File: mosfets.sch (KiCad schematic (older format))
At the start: 79 parts, among them P5 TERMINAL_BLOCK, P6 TERMINAL_BLOCK, Q1 2N7002P, Q10 2N7002P, Q11 2N7002P, Q12 BC846BPDW1, Q13 BC846BPDW1, Q14 SI2318CDS-T1-GE3, Q15 IRFB7545PbF, Q16 2N7002P, Q17 2N7002P, Q18 BC846BPDW1, Q19 BC846BPDW1, Q2 2N7002P, Q20 SI2318CDS-T1-GE3, Q21 IRFB7545PbF, Q3 2N7002P, Q4 BC846BPDW1, Q5 BC846BPDW1, Q6 BC846BPDW1, Q7 IRFB7545PbF, Q8 SI2318CDS-T1-GE3, Q9 IRFB7545PbF

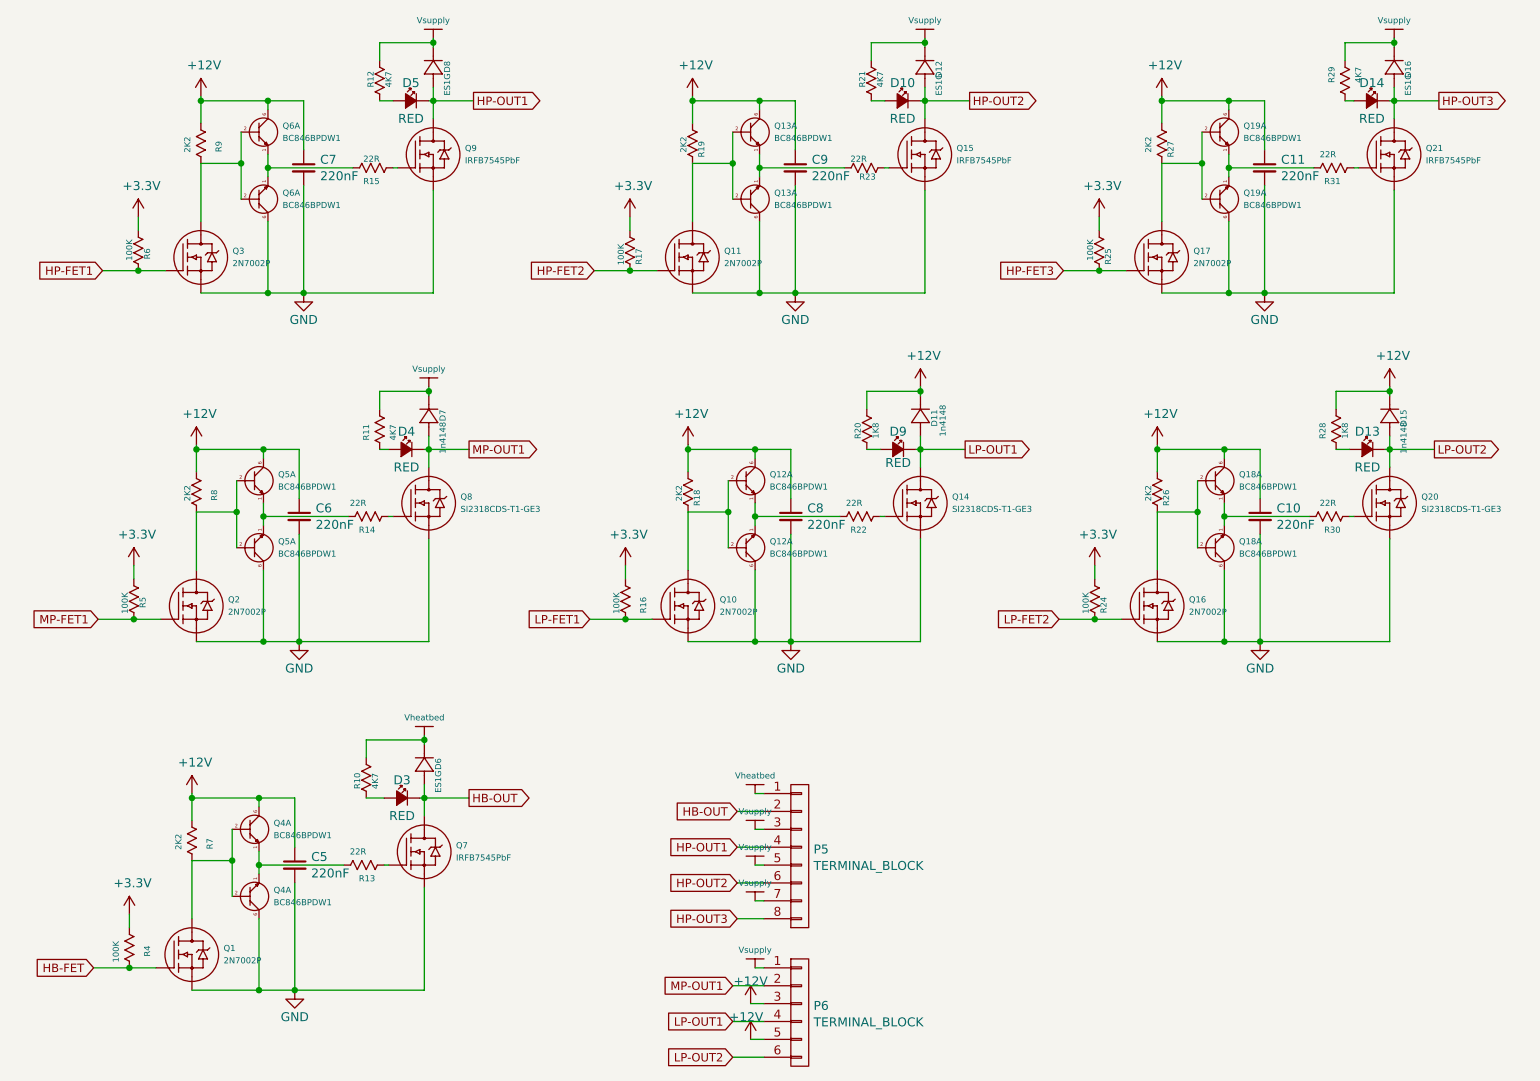
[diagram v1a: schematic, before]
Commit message: - Fix si2318 pinout - Fix slot problem introduced with attribute changes
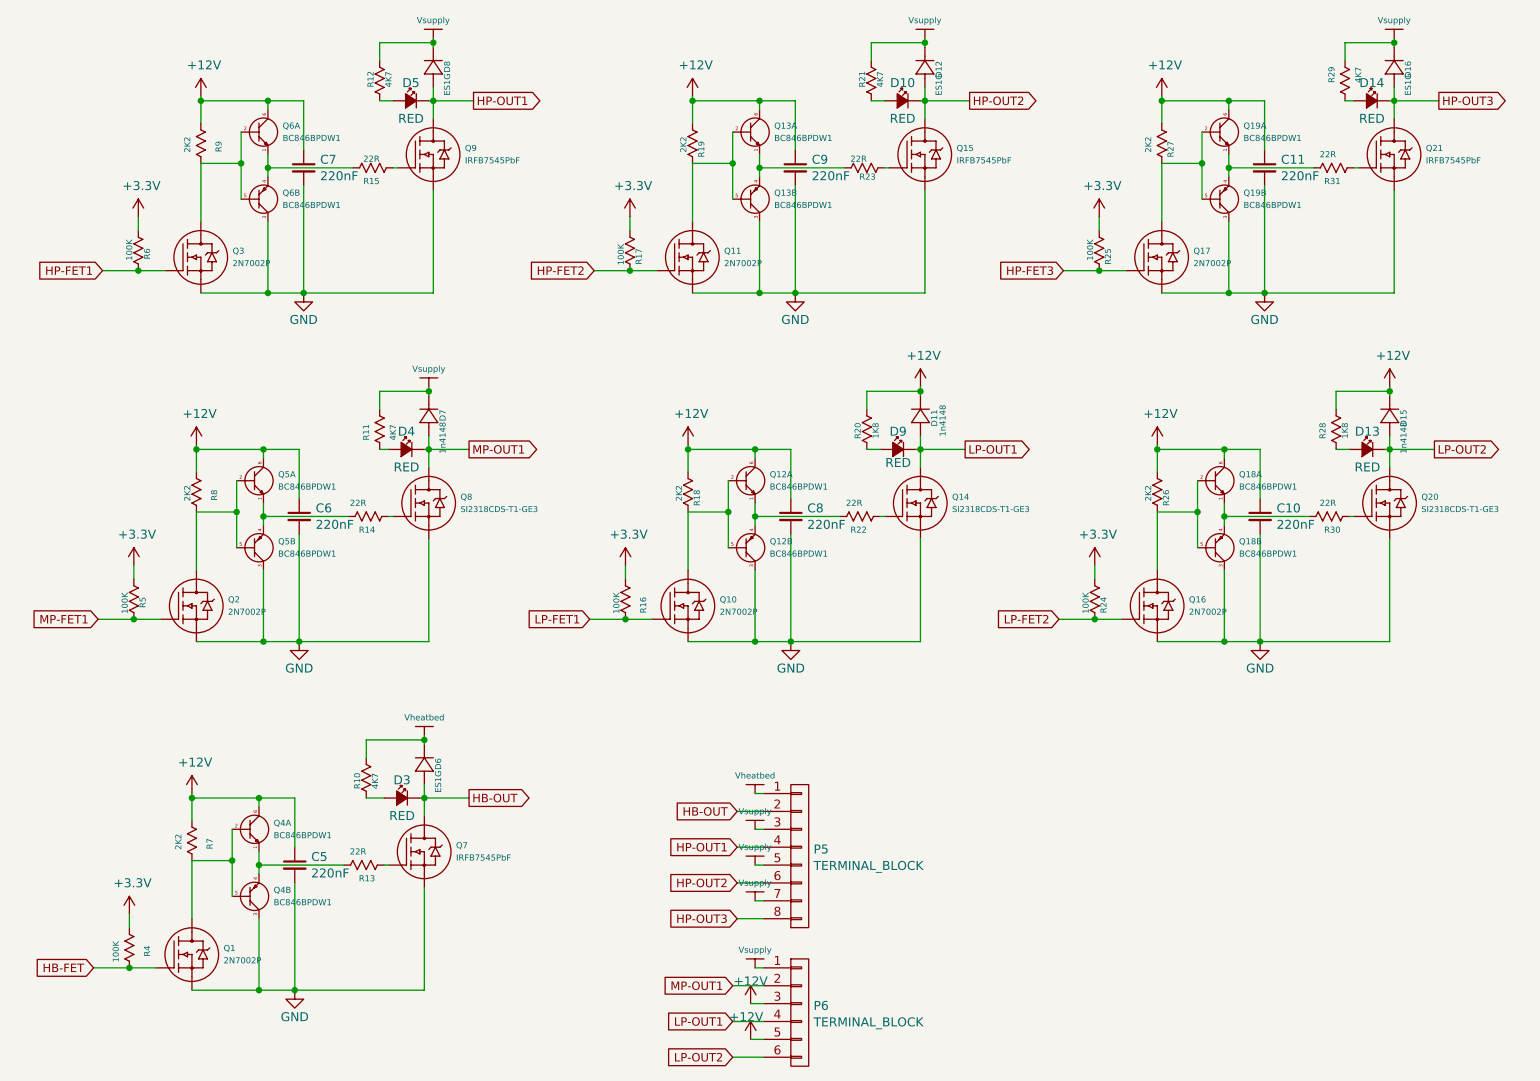
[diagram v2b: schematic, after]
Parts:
- removed Q14, Q20, Q8: SI2318CDS-T1-GE3, sot:SOT23_3L, symbol DMN3404L
- added Q14, Q20, Q8: SI2318CDS-T1-GE3, sot:SOT23_3L, symbol si2318cds
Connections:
- net GND: now also Q12.3 (C), Q13.3 (C), Q18.3 (C), Q19.3 (C), Q4.3 (C), Q5.3 (C), Q6.3 (C), Q14.2 (S), Q20.2 (S), Q8.2 (S); no longer Q12.6 (C), Q13.6 (C), Q18.6 (C), Q19.6 (C), Q4.6 (C), Q5.6 (C), Q6.6 (C)
- net LP-OUT1: now also Q14.3 (D)
- net LP-OUT2: now also Q20.3 (D)
- net MP-OUT1: now also Q8.3 (D)
- net at Q3.3 (D), Q6.2 (B), R9.1: now also Q6.5 (B); no longer Q6.2 (B)
- net at Q6.1 (E), R15.1: now also Q6.4 (E); no longer Q6.1 (E)
- net at Q11.3 (D), Q13.2 (B), R19.1: now also Q13.5 (B); no longer Q13.2 (B)
- net at Q13.1 (E), R23.1: now also Q13.4 (E); no longer Q13.1 (E)
- net at Q17.3 (D), Q19.2 (B), R27.1: now also Q19.5 (B); no longer Q19.2 (B)
- net at Q19.1 (E), R31.1: now also Q19.4 (E); no longer Q19.1 (E)
- net at Q1.3 (D), Q4.2 (B), R7.1: now also Q4.5 (B); no longer Q4.2 (B)
- net at Q4.1 (E), R13.1: now also Q4.4 (E); no longer Q4.1 (E)
- net at Q2.3 (D), Q5.2 (B), R8.1: now also Q5.5 (B); no longer Q5.2 (B)
- net at Q5.1 (E), R14.1: now also Q5.4 (E); no longer Q5.1 (E)
- net at R14.2: now also Q8.1 (G)
- net at Q10.3 (D), Q12.2 (B), R18.1: now also Q12.5 (B); no longer Q12.2 (B)
- net at Q12.1 (E), R22.1: now also Q12.4 (E); no longer Q12.1 (E)
- net at R22.2: now also Q14.1 (G)
- net at Q16.3 (D), Q18.2 (B), R26.1: now also Q18.5 (B); no longer Q18.2 (B)
- net at Q18.1 (E), R30.1: now also Q18.4 (E); no longer Q18.1 (E)
- net at R30.2: now also Q20.1 (G)
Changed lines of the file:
@@
 $Comp
 L BC846BPDW1 Q6
-U 1 1 568AF2DE
+U 2 1 568AF2DE
 P 2050 1625
 F 0 "Q6" H 2282 1715 34  0000 L CNN
@@
 F 4 "BC846BPDW1T1G" H 2050 1625 135 0001 L CNN "ManufacturerNo"
 F 5 "On Semiconductor" H 2050 1625 135 0001 L CNN "Manufacturer"
-	1    2050 1625
+	2    2050 1625
 	1    0    0    1
 $EndComp
@@
 $EndComp
 $Comp
-L Vsupply #P10
+L Vsupply #P11
 U 1 1 568AFFE8
 P 3125 700
-F 0 "#P10" H 3125 700 60  0001 C CNN
+F 0 "#P11" H 3125 700 60  0001 C CNN
 F 1 "Vsupply" H 3125 650 34  0000 C CNN
 F 2 "" H 3125 700 60  0000 C CNN
@@
 $Comp
 L BC846BPDW1 Q19
-U 1 1 568B2428
+U 2 1 568B2428
 P 7425 1625
 F 0 "Q19" H 7657 1715 34  0000 L CNN
@@
 F 4 "BC846BPDW1T1G" H 7425 1625 135 0001 L CNN "ManufacturerNo"
 F 5 "On Semiconductor" H 7425 1625 135 0001 L CNN "Manufacturer"
-	1    7425 1625
+	2    7425 1625
 	1    0    0    1
 $EndComp
@@
 $EndComp
 $Comp
-L Vsupply #P17
+L Vsupply #P18
 U 1 1 568B248A
 P 8500 700
-F 0 "#P17" H 8500 700 60  0001 C CNN
+F 0 "#P18" H 8500 700 60  0001 C CNN
 F 1 "Vsupply" H 8500 650 34  0000 C CNN
 F 2 "" H 8500 700 60  0000 C CNN
@@
 $Comp
 L BC846BPDW1 Q4
-U 1 1 568B41D4
+U 2 1 568B41D4
 P 2000 5525
 F 0 "Q4" H 2232 5615 34  0000 L CNN
@@
 F 4 "On Semiconductor" H 2000 5525 135 0001 L CNN "Manufacturer"
 F 5 "BC846BPDW1T1G" H 2000 5525 135 0001 L CNN "ManufacturerNo"
-	1    2000 5525
+	2    2000 5525
 	1    0    0    1
 $EndComp
@@
 $EndComp
 $Comp
-L Vheatbed #P8
+L Vheatbed #P9
 U 1 1 568B479B
 P 3075 4600
-F 0 "#P8" H 3075 4600 60  0001 C CNN
+F 0 "#P9" H 3075 4600 60  0001 C CNN
 F 1 "Vheatbed" H 3075 4550 34  0000 C CNN
 F 2 "" H 3075 4600 60  0000 C CNN
@@
 $Comp
 L BC846BPDW1 Q5
-U 1 1 568B79AD
+U 2 1 568B79AD
 P 2025 3575
 F 0 "Q5" H 2257 3665 34  0000 L CNN
@@
 F 4 "BC846BPDW1T1G" H 2025 3575 135 0001 L CNN "ManufacturerNo"
 F 5 "On Semiconductor" H 2025 3575 135 0001 L CNN "Manufacturer"
-	1    2025 3575
+	2    2025 3575
 	1    0    0    1
 $EndComp
@@
 $EndComp
 $Comp
-L Vsupply #P9
+L Vsupply #P10
 U 1 1 568B7A06
 P 3100 2650
-F 0 "#P9" H 3100 2650 60  0001 C CNN
+F 0 "#P10" H 3100 2650 60  0001 C CNN
 F 1 "Vsupply" H 3100 2600 34  0000 C CNN
 F 2 "" H 3100 2650 60  0000 C CNN
@@
 $Comp
 L BC846BPDW1 Q12
-U 1 1 568B7A20
+U 2 1 568B7A20
 P 4775 3575
 F 0 "Q12" H 5007 3665 34  0000 L CNN
@@
 F 4 "BC846BPDW1T1G" H 4775 3575 135 0001 L CNN "ManufacturerNo"
 F 5 "On Semiconductor" H 4775 3575 135 0001 L CNN "Manufacturer"
-	1    4775 3575
+	2    4775 3575
 	1    0    0    1
 $EndComp
@@
 $Comp
 L BC846BPDW1 Q18
-U 1 1 568B7A93
+U 2 1 568B7A93
 P 7400 3575
 F 0 "Q18" H 7632 3665 34  0000 L CNN
@@
 F 4 "BC846BPDW1T1G" H 7400 3575 135 0001 L CNN "ManufacturerNo"
 F 5 "On Semiconductor" H 7400 3575 135 0001 L CNN "Manufacturer"
-	1    7400 3575
+	2    7400 3575
 	1    0    0    1
 $EndComp
@@
 $EndComp
 $Comp
-L DMN3404L Q8
-U 1 1 568B81E9
-P 2900 3650
-F 0 "Q8" H 3277 3885 34  0000 L CNN
-F 1 "SI2318CDS-T1-GE3" H 3277 3816 34  0000 L CNN
-F 2 "sot:SOT23_3L" H 2900 3650 60  0001 C CNN
-F 3 "" H 2900 3650 60  0000 C CNN
-F 4 "SI2318CDS-T1-GE3" H 2900 3650 135 0001 L CNN "ManufacturerNo"
-F 5 "Vishay" H 2900 3650 135 0001 L CNN "Manufacturer"
-	1    2900 3650
-	1    0    0    -1
-$EndComp
-$Comp
 L 1n4148-RESCUE-rados D11
 U 1 1 568B8B88
@@
 	1    8525 3075
 	0    -1   -1   0
-$EndComp
-$Comp
-L DMN3404L Q14
-U 1 1 568B9231
-P 5650 3650
-F 0 "Q14" H 6027 3885 34  0000 L CNN
-F 1 "SI2318CDS-T1-GE3" H 6027 3816 34  0000 L CNN
-F 2 "sot:SOT23_3L" H 5650 3650 60  0001 C CNN
-F 3 "" H 5650 3650 60  0000 C CNN
-F 4 "SI2318CDS-T1-GE3" H 5650 3650 135 0001 L CNN "ManufacturerNo"
-F 5 "Vishay" H 5650 3650 135 0001 L CNN "Manufacturer"
-	1    5650 3650
-	1    0    0    -1
-$EndComp
-$Comp
-L DMN3404L Q20
-U 1 1 568B9365
-P 8275 3650
-F 0 "Q20" H 8652 3885 34  0000 L CNN
-F 1 "SI2318CDS-T1-GE3" H 8652 3816 34  0000 L CNN
-F 2 "sot:SOT23_3L" H 8275 3650 60  0001 C CNN
-F 3 "" H 8275 3650 60  0000 C CNN
-F 4 "SI2318CDS-T1-GE3" H 8275 3650 135 0001 L CNN "ManufacturerNo"
-F 5 "Vishay" H 8275 3650 135 0001 L CNN "Manufacturer"
-	1    8275 3650
-	1    0    0    -1
 $EndComp
 $Comp
@@
 $EndComp
 $Comp
-L Vheatbed #P11
+L Vheatbed #P12
 U 1 1 568B0A81
 P 4925 4925
-F 0 "#P11" H 4925 4925 60  0001 C CNN
+F 0 "#P12" H 4925 4925 60  0001 C CNN
 F 1 "Vheatbed" H 4925 4875 34  0000 C CNN
 F 2 "" H 4925 4925 60  0000 C CNN
@@
 $EndComp
 $Comp
-L Vsupply #P12
+L Vsupply #P13
 U 1 1 568B0DA2
 P 4925 5125
-F 0 "#P12" H 4925 5125 60  0001 C CNN
+F 0 "#P13" H 4925 5125 60  0001 C CNN
 F 1 "Vsupply" H 4925 5075 34  0000 C CNN
 F 2 "" H 4925 5125 60  0000 C CNN
@@
 $EndComp
 $Comp
-L Vsupply #P13
+L Vsupply #P14
 U 1 1 568B1161
 P 4925 5325
-F 0 "#P13" H 4925 5325 60  0001 C CNN
+F 0 "#P14" H 4925 5325 60  0001 C CNN
 F 1 "Vsupply" H 4925 5275 34  0000 C CNN
 F 2 "" H 4925 5325 60  0000 C CNN
@@
 HP-OUT1
 $Comp
-L Vsupply #P14
+L Vsupply #P15
 U 1 1 568BBE8C
 P 4925 5525
-F 0 "#P14" H 4925 5525 60  0001 C CNN
+F 0 "#P15" H 4925 5525 60  0001 C CNN
 F 1 "Vsupply" H 4925 5475 34  0000 C CNN
 F 2 "" H 4925 5525 60  0000 C CNN
@@
 HP-OUT3
 $Comp
-L Vsupply #P15
+L Vsupply #P16
 U 1 1 568BDAE4
 P 4925 5900
-F 0 "#P15" H 4925 5900 60  0001 C CNN
+F 0 "#P16" H 4925 5900 60  0001 C CNN
 F 1 "Vsupply" H 4925 5850 34  0000 C CNN
 F 2 "" H 4925 5900 60  0000 C CNN
@@
 $EndComp
 $Comp
-L Vsupply #P16
+L Vsupply #P17
 U 1 1 568B1D38
 P 5875 700
-F 0 "#P16" H 5875 700 60  0001 C CNN
+F 0 "#P17" H 5875 700 60  0001 C CNN
 F 1 "Vsupply" H 5875 650 34  0000 C CNN
 F 2 "" H 5875 700 60  0000 C CNN
@@
 $Comp
 L BC846BPDW1 Q13
-U 1 1 568B1CD6
+U 2 1 568B1CD6
 P 4800 1625
 F 0 "Q13" H 5032 1715 34  0000 L CNN
@@
 F 4 "BC846BPDW1T1G" H 4800 1625 135 0001 L CNN "ManufacturerNo"
 F 5 "On Semiconductor" H 4800 1625 135 0001 L CNN "Manufacturer"
-	1    4800 1625
+	2    4800 1625
 	1    0    0    1
 $EndComp
@@
 	1    0    0    -1
 $EndComp
+$Comp
+L si2318cds Q8
+U 1 1 56EAF7B5
+P 2900 3650
+F 0 "Q8" H 3277 3884 34  0000 L CNN
+F 1 "SI2318CDS-T1-GE3" H 3277 3815 33  0000 L CNN
+F 2 "sot:SOT23_3L" H 2900 3650 60  0001 C CNN
+F 3 "" H 2900 3650 60  0000 C CNN
+F 4 "unlimited" H 2900 4262 34  0001 L BNN "use-license"
+F 5 "Stefan Salewski, Armin van der Togt" H 2900 4062 34  0001 L BNN "author"
+F 6 "40V 5.6A N-channel MOSFET" H 2900 4112 34  0001 L BNN "description"
+F 7 "GPL" H 2900 4212 34  0001 L BNN "dist-license"
+	1    2900 3650
+	1    0    0    -1
+$EndComp
+$Comp
+L si2318cds Q14
+U 1 1 56EB003F
+P 5650 3650
+F 0 "Q14" H 6027 3884 34  0000 L CNN
+F 1 "SI2318CDS-T1-GE3" H 6027 3815 33  0000 L CNN
+F 2 "sot:SOT23_3L" H 5650 3650 60  0001 C CNN
+F 3 "" H 5650 3650 60  0000 C CNN
+F 4 "unlimited" H 5650 4262 34  0001 L BNN "use-license"
+F 5 "Stefan Salewski, Armin van der Togt" H 5650 4062 34  0001 L BNN "author"
+F 6 "40V 5.6A N-channel MOSFET" H 5650 4112 34  0001 L BNN "description"
+F 7 "GPL" H 5650 4212 34  0001 L BNN "dist-license"
+	1    5650 3650
+	1    0    0    -1
+$EndComp
+$Comp
+L si2318cds Q20
+U 1 1 56EB03AB
+P 8275 3650
+F 0 "Q20" H 8652 3884 34  0000 L CNN
+F 1 "SI2318CDS-T1-GE3" H 8652 3815 33  0000 L CNN
+F 2 "sot:SOT23_3L" H 8275 3650 60  0001 C CNN
+F 3 "" H 8275 3650 60  0000 C CNN
+F 4 "unlimited" H 8275 4262 34  0001 L BNN "use-license"
+F 5 "Stefan Salewski, Armin van der Togt" H 8275 4062 34  0001 L BNN "author"
+F 6 "40V 5.6A N-channel MOSFET" H 8275 4112 34  0001 L BNN "description"
+F 7 "GPL" H 8275 4212 34  0001 L BNN "dist-license"
+	1    8275 3650
+	1    0    0    -1
+$EndComp
